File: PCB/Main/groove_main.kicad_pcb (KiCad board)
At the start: 2 copper layers, 214 x 99 mm, 38 parts, among them J1 Left_X, J2 Left_Y, J3 Right_X, J4 Right_Y, J5 Left_X, J6 Left_Y, J7 Right_X, J8 Right_Y, U2 Pico, U3 CD4052B

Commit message: Main PCB progress 50%
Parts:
- removed D20, D21, D22, D23, D24: WS2812B_Unified, groove_pico:WS2812B-2835
- added C1: 0.1uF, Capacitor_SMD:C_0603_1608Metric_Pad1.08x0.95mm_HandSolder, F.Cu at (32.5, 102.5)
- added C2: 0.1uF, Capacitor_SMD:C_0603_1608Metric_Pad1.08x0.95mm_HandSolder, F.Cu at (98.2, 125.0)
- added C3: 0.1uF, Capacitor_SMD:C_0603_1608Metric_Pad1.08x0.95mm_HandSolder, B.Cu at (121.3, 65.2)
- added C4: 0.1uF, Capacitor_SMD:C_0603_1608Metric_Pad1.08x0.95mm_HandSolder, F.Cu at (144.6, 97.4)
- added C5: 0.1uF, Capacitor_SMD:C_0603_1608Metric_Pad1.08x0.95mm_HandSolder, F.Cu at (175.1, 130.9)
- added C6: 0.1uF, Capacitor_SMD:C_0603_1608Metric_Pad1.08x0.95mm_HandSolder, F.Cu at (235.4, 96.5)
- added C7: 0.1uF, Capacitor_SMD:C_0603_1608Metric_Pad1.08x0.95mm_HandSolder, F.Cu at (69.7, 118.3)
- added C8: 0.1uF, Capacitor_SMD:C_0603_1608Metric_Pad1.08x0.95mm_HandSolder, F.Cu at (203.0, 118.7)
- added C9: 0.1uF, Capacitor_SMD:C_0603_1608Metric_Pad1.08x0.95mm_HandSolder, F.Cu at (127.3, 73.4)
- added J10: Left_Y, groove_pico:Solder_3P_S, F.Cu at (73.3, 77.9)
- added J11: Right_X, groove_pico:Solder_3P_S, F.Cu at (197.3, 77.9)
- added J12: Right_Y, groove_pico:Solder_3P_S, F.Cu at (188.3, 77.9)
- added J9: Left_X, groove_pico:Solder_3P_S, F.Cu at (82.3, 77.9)
- added SW1: SWITCH_SPST, groove_pico:EVQP1K05M, F.Cu at (118.3, 88.4)
- added SW2: SWITCH_SPST, groove_pico:EVQP1K05M, F.Cu at (135.3, 88.4)
- added SW3: SWITCH_SPST, groove_pico:EVQP1K05M, F.Cu at (152.3, 88.4)
- added U3: LM4040DBZ-3, Package_TO_SOT_SMD:SOT-23, B.Cu at (128.3, 65.2)
- J1, J2, J3, J4: footprint Connector_PinHeader_1.27mm:PinHeader_1x03_P1.27mm_Vertical -> groove_pico:SH1.25_Thruhole_3P
- J5, J6, J7, J8: footprint Connector_JST:JST_GH_BM03B-GHS-TBT_1x03-1MP_P1.25mm_Vertical -> groove_pico:SH1.25mm_3P_SMD
- R2, R3: moved to B.Cu
- U2: renamed from U3; moved to B.Cu
- moved J8 111.3 mm to (188.3, 83.4), turned to 180 degrees
- moved J7 110.4 mm to (197.3, 83.4), turned to 180 degrees
- moved U2 81.0 mm to (119.3, 61.4)
- moved J5 56.2 mm to (82.3, 83.4), turned to 180 degrees
- moved J6 47.9 mm to (73.3, 83.4), turned to 180 degrees
- moved R2 17.0 mm to (129.3, 60.4), turned to 180 degrees
- moved U1 8.89 mm to (117.3, 81.4)
- moved D8 7.20 mm to (89.4, 89.3), turned to -45 degrees
- moved D19 5.53 mm to (229.4, 89.3), turned to -45 degrees
- moved R3 5.37 mm to (141.3, 60.4)
- moved D14 4.67 mm to (171.3, 113.4)
- moved R1 4.22 mm to (69.0, 71.3)
- moved D2 3.18 mm to (41.3, 89.3)
- moved D6 2.96 mm to (89.4, 137.4), turned to -135 degrees
- moved D17 2.62 mm to (229.4, 137.4), turned to -135 degrees
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- renumbered U2 to U1
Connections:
- D19 pad O: Net-(D19-Out) -> unconnected-(D19-Out-PadO)
- J1 pad 1: +3.3VADC -> GNDREF
- J1 pad 3: GND -> +3.3VADC
- J2 pad 1: +3.3VADC -> GNDREF
- J2 pad 3: GND -> +3.3VADC
- J3 pad 1: +3.3VADC -> GNDREF
- J3 pad 3: GND -> +3.3VADC
- J4 pad 1: +3.3VADC -> GNDREF
- J4 pad 3: GND -> +3.3VADC
- J5 pad 1: +3.3VADC -> GNDREF
- J5 pad 3: GND -> +3.3VADC
- J6 pad 1: +3.3VADC -> GNDREF
- J6 pad 3: GND -> +3.3VADC
- J7 pad 1: +3.3VADC -> GNDREF
- J7 pad 3: GND -> +3.3VADC
- J8 pad 1: +3.3VADC -> GNDREF
- J8 pad 3: GND -> +3.3VADC
- U1 pad 34: unconnected-(U2-GPIO28_ADC2-Pad34) -> GNDREF
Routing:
- net +5V: track 0.00 -> 513.2 mm
- net +3.3VADC: track 0.00 -> 191.1 mm, vias 0 -> 3
- net GNDREF: track 0.00 -> 186.6 mm, vias 0 -> 3
- net /RX: track 0.00 -> 95.6 mm, vias 0 -> 1
- net /RY: track 0.00 -> 91.1 mm, vias 0 -> 1
- net /LY: track 0.00 -> 67.0 mm, vias 0 -> 2
- net /LX: track 0.00 -> 64.4 mm, vias 0 -> 2
- net Net-(D11-Out): track 0.00 -> 62.9 mm, vias 0 -> 2
- net Net-(D8-Out): track 0.00 -> 37.7 mm
- net Net-(USB1-DP1): track 0.00 -> 35.0 mm
- net Net-(USB1-DN1): track 0.00 -> 34.8 mm
- net Net-(D12-Out): track 0.00 -> 32.3 mm, vias 0 -> 2
- net +3V3: track 0.00 -> 27.7 mm
- net Net-(U1-GPIO20): track 0.00 -> 25.5 mm
- net Net-(D4-Out): track 0.00 -> 25.0 mm
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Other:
- outline, holes or cut-outs redrawn

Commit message: Main PCB progress 70%
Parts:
- added D20: WS2812B_Unified, groove_pico:WS2812B-4020, B.Cu at (70.4, 126.1)
- added D21: WS2812B_Unified, groove_pico:WS2812B-4020, B.Cu at (60.2, 126.1)
- added D22: WS2812B_Unified, groove_pico:WS2812B-4020, B.Cu at (52.6, 118.5)
- added D23: WS2812B_Unified, groove_pico:WS2812B-4020, B.Cu at (52.6, 108.3)
- added D24: WS2812B_Unified, groove_pico:WS2812B-4020, B.Cu at (60.2, 100.7)
- added D25: WS2812B_Unified, groove_pico:WS2812B-4020, B.Cu at (70.4, 100.7)
- added D26: WS2812B_Unified, groove_pico:WS2812B-4020, B.Cu at (78.0, 108.3)
- added D27: WS2812B_Unified, groove_pico:WS2812B-4020, B.Cu at (78.0, 118.5)
- added D28: WS2812B_Unified, groove_pico:WS2812B-4020_UP, F.Cu at (76.1, 113.4)
- added D29: WS2812B_Unified, groove_pico:WS2812B-4020_UP, F.Cu at (65.3, 102.6)
- added D30: WS2812B_Unified, groove_pico:WS2812B-4020_UP, F.Cu at (54.5, 113.4)
- added D31: WS2812B_Unified, groove_pico:WS2812B-4020_UP, F.Cu at (65.3, 124.2)
- added D32: WS2812B_Unified, groove_pico:WS2812B-4020, B.Cu at (210.4, 126.1)
- added D33: WS2812B_Unified, groove_pico:WS2812B-4020, B.Cu at (200.2, 126.1)
- added D34: WS2812B_Unified, groove_pico:WS2812B-4020, B.Cu at (192.6, 118.5)
- added D35: WS2812B_Unified, groove_pico:WS2812B-4020, B.Cu at (192.6, 108.3)
- added D36: WS2812B_Unified, groove_pico:WS2812B-4020, B.Cu at (200.2, 100.7)
- added D37: WS2812B_Unified, groove_pico:WS2812B-4020, B.Cu at (210.4, 100.7)
- added D38: WS2812B_Unified, groove_pico:WS2812B-4020, B.Cu at (218.0, 108.3)
- added D39: WS2812B_Unified, groove_pico:WS2812B-4020, B.Cu at (218.0, 118.5)
- added D40: WS2812B_Unified, groove_pico:WS2812B-4020_UP, F.Cu at (216.1, 113.4)
- added D41: WS2812B_Unified, groove_pico:WS2812B-4020_UP, F.Cu at (205.3, 102.6)
- added D42: WS2812B_Unified, groove_pico:WS2812B-4020_UP, F.Cu at (194.5, 113.4)
- added D43: WS2812B_Unified, groove_pico:WS2812B-4020_UP, F.Cu at (205.3, 124.2)
- added J13: SW, groove_pico:Solder_1P, B.Cu at (69.1, 107.3)
- added J14: SW, groove_pico:Solder_1P, B.Cu at (209.1, 107.3)
- added J15: V, groove_pico:Solder_1P, B.Cu at (59.0, 110.4)
- added J16: LED, groove_pico:Solder_1P, B.Cu at (72.7, 119.2)
- added J18: G, groove_pico:Solder_1P, B.Cu at (62.5, 107.5)
- added J19: V, groove_pico:Solder_1P, B.Cu at (199.0, 110.4)
- added J20: LED, groove_pico:Solder_1P, B.Cu at (212.7, 119.2)
- added J22: G, groove_pico:Solder_1P, B.Cu at (202.5, 107.5)
- added R4: 10, Resistor_SMD:R_0603_1608Metric, F.Cu at (41.8, 43.5)
- added R5: 10, Resistor_SMD:R_0603_1608Metric, F.Cu at (41.8, 46.0)
- added SCR1: ScrewHole, groove_pico:Hole2.0, F.Cu at (65.3, 100.2)
- added SCR2: ScrewHole, groove_pico:Hole2.0, F.Cu at (78.5, 113.4)
- added SCR3: ScrewHole, groove_pico:Hole2.0, F.Cu at (65.3, 126.6)
- added SCR4: ScrewHole, groove_pico:Hole2.0, F.Cu at (52.1, 113.4)
- added SCR5: ScrewHole, groove_pico:Hole2.0, F.Cu at (205.3, 100.2)
- added SCR6: ScrewHole, groove_pico:Hole2.0, F.Cu at (218.5, 113.4)
- added SCR7: ScrewHole, groove_pico:Hole2.0, F.Cu at (205.3, 126.6)
- added SCR8: ScrewHole, groove_pico:Hole2.0, F.Cu at (192.1, 113.4)
- added SW4: SWITCH_SPST, groove_pico:SW_Kailh_Choc_V1V2_1.00u_LED, F.Cu at (65.3, 113.4)
- added SW5: SWITCH_SPST, groove_pico:SW_Kailh_Choc_V1V2_1.00u_LED, F.Cu at (205.3, 113.4)
- moved C7 16.1 mm to (65.2, 133.8)
- moved C8 12.9 mm to (205.5, 131.4)
- moved C9 2.06 mm to (126.3, 71.6)
- renumbered R2 to R1, R3 to R2, R1 to R3
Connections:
- SW1 pad 1: unconnected-(SW1-"~{"}-Pad1) -> Net-(U1-GPIO0)
- SW1 pad 2: unconnected-(SW1-"~{"}-Pad2) -> GND
- SW2 pad 1: unconnected-(SW2-"~{"}-Pad1) -> Net-(U1-GPIO1)
- SW2 pad 2: unconnected-(SW2-"~{"}-Pad2) -> GND
- SW3 pad 1: unconnected-(SW3-"~{"}-Pad1) -> Net-(U1-GPIO2)
- SW3 pad 2: unconnected-(SW3-"~{"}-Pad2) -> GND
- U1 pad 1: unconnected-(U1-GPIO0-Pad1) -> Net-(U1-GPIO0)
- U1 pad 13: unconnected-(U1-GND-Pad13) -> GND
- U1 pad 15: unconnected-(U1-GPIO11-Pad15) -> Net-(U1-GPIO11)
- U1 pad 16: /RGB -> Net-(U1-GPIO12)
- U1 pad 17: unconnected-(U1-GPIO13-Pad17) -> /RGB
- U1 pad 2: unconnected-(U1-GPIO1-Pad2) -> Net-(U1-GPIO1)
- U1 pad 23: unconnected-(U1-GND-Pad23) -> GND
- U1 pad 33: unconnected-(U1-AGND-Pad33) -> GNDREF
- U1 pad 34: GNDREF -> unconnected-(U1-GPIO28_ADC2-Pad34)
- U1 pad 4: unconnected-(U1-GPIO2-Pad4) -> Net-(U1-GPIO2)
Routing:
- net +5V: track 513.2 -> 796.8 mm, vias 0 -> 2
- net Net-(D30-Out): track 0.00 -> 16.5 mm
- net Net-(D40-Out): track 0.00 -> 16.5 mm
- net Net-(D28-Out): track 0.00 -> 16.5 mm
- net Net-(D42-Out): track 0.00 -> 16.5 mm
- net Net-(D41-Out): track 0.00 -> 16.3 mm
- net Net-(D29-Out): track 0.00 -> 16.3 mm
- net GND: track 9.07 -> 20.2 mm, vias 6 -> 18
- net Net-(D23-Out): track 0.00 -> 10.6 mm
- net Net-(D35-Out): track 0.00 -> 10.6 mm
- net Net-(D33-Out): track 0.00 -> 10.6 mm
- net Net-(D21-Out): track 0.00 -> 10.6 mm
- net Net-(D37-Out): track 0.00 -> 10.6 mm
- net Net-(D25-Out): track 0.00 -> 10.6 mm
- net Net-(D38-Out): track 0.00 -> 10.1 mm
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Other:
- outline, holes or cut-outs redrawn

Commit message: Main PCB progress 85%
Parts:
- added J17: LED, groove_pico:Solder_1P_S, F.Cu at (59.3, 85.4)
- added J21: LED, groove_pico:Solder_1P_S, F.Cu at (211.3, 85.4)
- added J23: SW, groove_pico:Solder_1P_S, F.Cu at (205.3, 85.4)
- added J24: SW, groove_pico:Solder_1P_S, F.Cu at (65.3, 85.4)
- added J25: V, groove_pico:Solder_1P_S, F.Cu at (214.3, 85.4)
- added J26: V, groove_pico:Solder_1P_S, F.Cu at (56.3, 85.4)
- added J27: G, groove_pico:Solder_1P_S, F.Cu at (62.3, 85.4)
- added J28: G, groove_pico:Solder_1P_S, F.Cu at (208.3, 85.4)
- C7, C8, C9: moved to B.Cu
- J13, J14, J15, J16, J18, J19, J20, J22: footprint groove_pico:Solder_1P -> groove_pico:Solder_1P_S
- moved R5 75.2 mm to (105.9, 85.4), turned to -90 degrees
- moved R4 74.4 mm to (103.3, 85.4), turned to -90 degrees
- moved R3 34.8 mm to (100.8, 85.4), turned to -90 degrees
- moved C7 26.8 mm to (60.1, 107.5)
- moved C8 24.5 mm to (200.0, 107.5)
- moved SW1 6.00 mm to (124.3, 88.4)
- moved SW3 6.00 mm to (146.3, 88.4)
- moved C9 5.92 mm to (128.5, 66.1)
- moved J20 2.93 mm to (211.2, 116.7), turned to -90 degrees
- moved J16 2.85 mm to (71.2, 116.8), turned to -90 degrees
- moved U3 1.75 mm to (128.4, 63.4)
- moved C4 1.64 mm to (143.1, 97.9)
- moved J13 1.01 mm to (68.3, 106.7), turned to 90 degrees
- moved D11 1.00 mm to (151.3, 96.4)
- moved D9 1.00 mm to (119.3, 96.4)
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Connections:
- net /RGB renamed Net-(U1-GPIO13)
- R4 pad 1: Net-(D20-In) -> Net-(J17-Pad1)
- R5 pad 1: Net-(D32-In) -> Net-(J21-Pad1)
- SW1 pad 1: Net-(U1-GPIO0) -> Net-(U1-GPIO2)
- SW3 pad 1: Net-(U1-GPIO2) -> Net-(U1-GPIO0)
- SW4 pad 1: Net-(J13-Pad1) -> GND
- SW4 pad 2: GND -> Net-(J13-Pad1)
- SW5 pad 1: Net-(J14-Pad1) -> GND
- SW5 pad 2: GND -> Net-(J14-Pad1)
- U1 pad 11: unconnected-(U1-GPIO8-Pad11) -> Net-(U1-GPIO8)
- U1 pad 12: unconnected-(U1-GPIO9-Pad12) -> Net-(U1-GPIO9)
- U1 pad 13: GND -> unconnected-(U1-GND-Pad13)
- U1 pad 40: unconnected-(U1-VBUS-Pad40) -> Net-(U1-VBUS)
- U1 pad 8: unconnected-(U1-GND-Pad8) -> GND
- U2 pad 6: unconnected-(U2-INH-Pad6) -> GND
- USB1 pad 11: Net-(USB1-VBUS-Pad11) -> Net-(U1-VBUS)
- USB1 pad 2: Net-(USB1-VBUS-Pad11) -> Net-(U1-VBUS)
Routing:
- net +5V: track 796.8 -> 1057.8 mm, vias 2 -> 8
- net Net-(J21-Pad1): track 0.00 -> 111.1 mm, vias 0 -> 2
- net Net-(U1-GPIO8): track 0.00 -> 98.1 mm, vias 0 -> 1
- net GND: track 20.2 -> 93.0 mm, vias 18 -> 80
- net Net-(U1-GPIO9): track 0.00 -> 53.3 mm, vias 0 -> 1
- net Net-(J17-Pad1): track 0.00 -> 51.0 mm, vias 0 -> 2
- net Net-(D1-In): track 0.00 -> 39.7 mm, vias 0 -> 2
- net Net-(U1-VBUS): track 0.00 -> 26.0 mm, vias 0 -> 2
- net Net-(U1-GPIO2): track 0.00 -> 18.4 mm, vias 0 -> 1
- net unconnected-(USB1-SHIELD-Pad13): track 0.00 -> 17.0 mm
- net Net-(U1-GPIO1): track 0.00 -> 15.5 mm, vias 0 -> 1
- net Net-(U1-GPIO0): track 0.00 -> 15.2 mm, vias 0 -> 1
- net GNDREF: track 187.3 -> 194.3 mm
- net +3.3VADC: track 190.6 -> 197.2 mm
- net Net-(USB1-CC2): track 5.54 -> 11.6 mm
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- added copper zone on B.Cu, net GND
- added copper zone on F.Cu, net GND

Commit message: Main PCB v1.0
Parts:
- added SCR10: ScrewHole, groove_pico:Hole2.0, F.Cu at (221.3, 81.4)
- added SCR11: ScrewHole, groove_pico:Hole2.0, F.Cu at (165.3, 59.4)
- added SCR12: ScrewHole, groove_pico:Hole2.0, F.Cu at (109.3, 97.4)
- added SCR13: ScrewHole, groove_pico:Hole2.0, F.Cu at (49.3, 81.4)
- added SCR14: ScrewHole, groove_pico:Hole2.0, F.Cu at (161.3, 97.4)
- added SCR15: ScrewHole, groove_pico:Hole2.0, F.Cu at (65.3, 141.4)
- added SCR16: ScrewHole, groove_pico:Hole2.0, F.Cu at (205.3, 141.4)
- added SCR9: ScrewHole, groove_pico:Hole2.0, F.Cu at (105.3, 59.4)
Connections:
- J13 pad 1: Net-(J13-Pad1) -> /SW_L
- J14 pad 1: Net-(J14-Pad1) -> /SW_R
- J17 pad 1: Net-(J17-Pad1) -> Net-(D20-In)
- J21 pad 1: Net-(J21-Pad1) -> Net-(D32-In)
- J23 pad 1: Net-(U1-GPIO8) -> /SW_R
- J24 pad 1: Net-(U1-GPIO9) -> /SW_L
- R4 pad 1: Net-(J17-Pad1) -> Net-(D20-In)
- R5 pad 1: Net-(J21-Pad1) -> Net-(D32-In)
- SW4 pad 2: Net-(J13-Pad1) -> /SW_L
- SW5 pad 2: Net-(J14-Pad1) -> /SW_R
- U1 pad 11: Net-(U1-GPIO8) -> /SW_R
- U1 pad 12: Net-(U1-GPIO9) -> /SW_L
- U1 pad 28: unconnected-(U1-GND-Pad28) -> GND
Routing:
- net Net-(D32-In): track 9.84 -> 178.5 mm, vias 0 -> 4
- net /SW_R: track 0.00 -> 131.8 mm, vias 0 -> 2
- net Net-(J21-Pad1): track 111.1 -> 0.00 mm, vias 2 -> 0
- net Net-(D20-In): track 9.74 -> 115.5 mm, vias 0 -> 4
- net Net-(U1-GPIO8): track 98.1 -> 0.00 mm, vias 1 -> 0
- net /SW_L: track 0.00 -> 87.8 mm, vias 0 -> 3
- net Net-(U1-GPIO9): track 53.3 -> 0.00 mm, vias 1 -> 0
- net Net-(J17-Pad1): track 51.0 -> 0.00 mm, vias 2 -> 0
- net +5V: track 1057.8 -> 1052.1 mm
- net Net-(J13-Pad1): track 4.49 -> 0.00 mm
- net Net-(J14-Pad1): track 4.39 -> 0.00 mm
- net Net-(D41-Out): track 16.3 -> 13.9 mm
- net Net-(D29-Out): track 16.3 -> 13.9 mm
- net Net-(D8-Out): track 38.6 -> 39.2 mm
- net GND: track 93.0 -> 93.2 mm, vias 80 -> 83
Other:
- board text added: "Groove Pico v1.0"

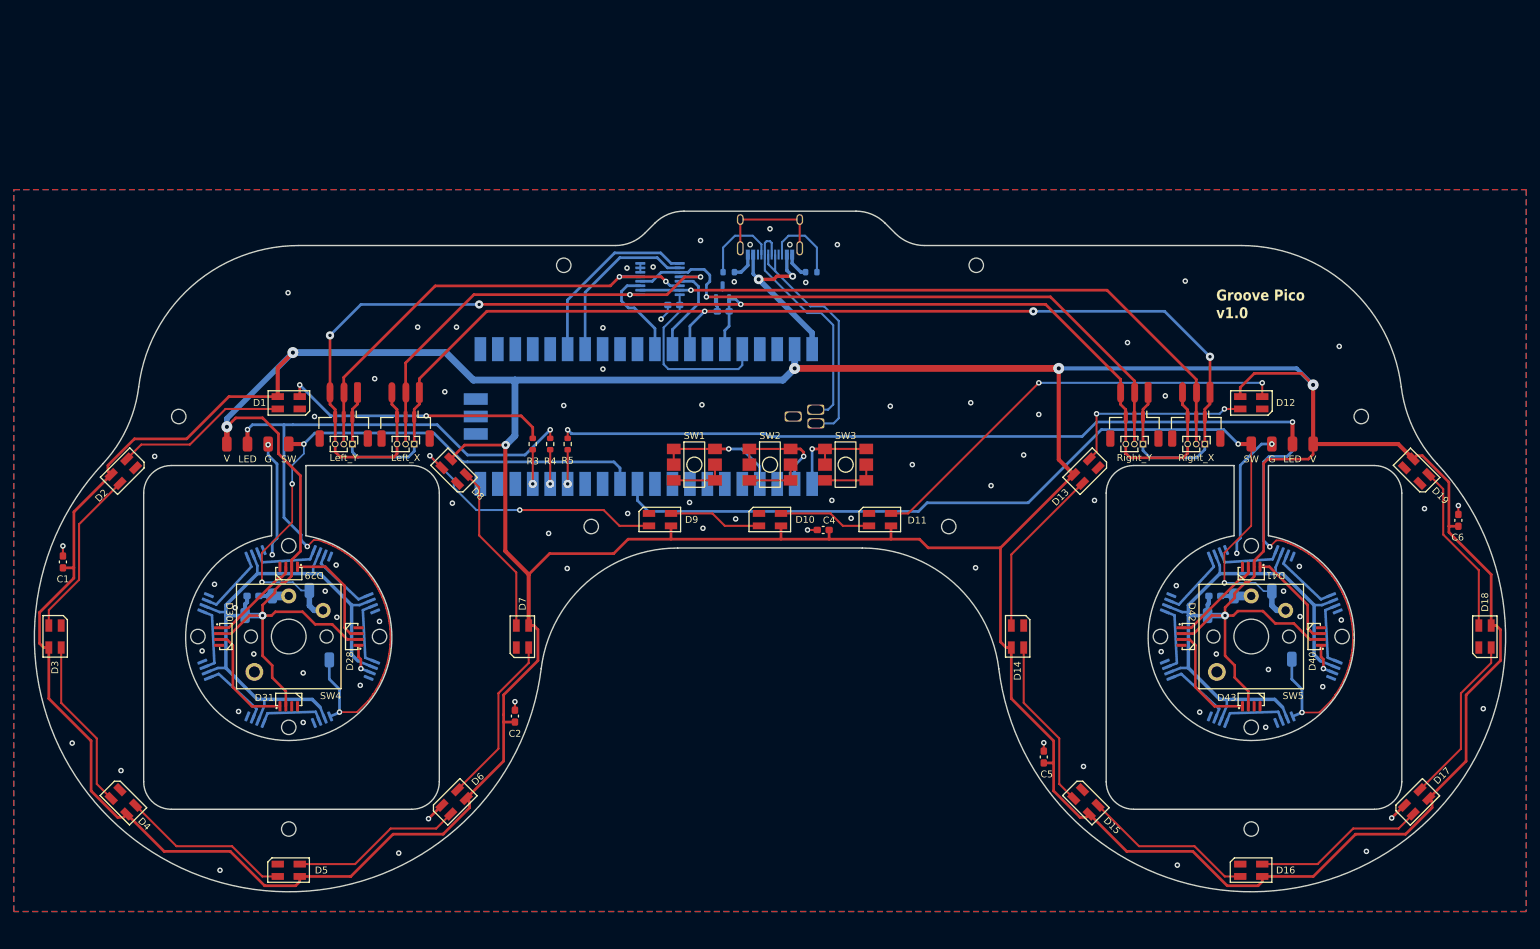
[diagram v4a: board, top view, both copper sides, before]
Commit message: Add slots in PCB for Hall gimbals
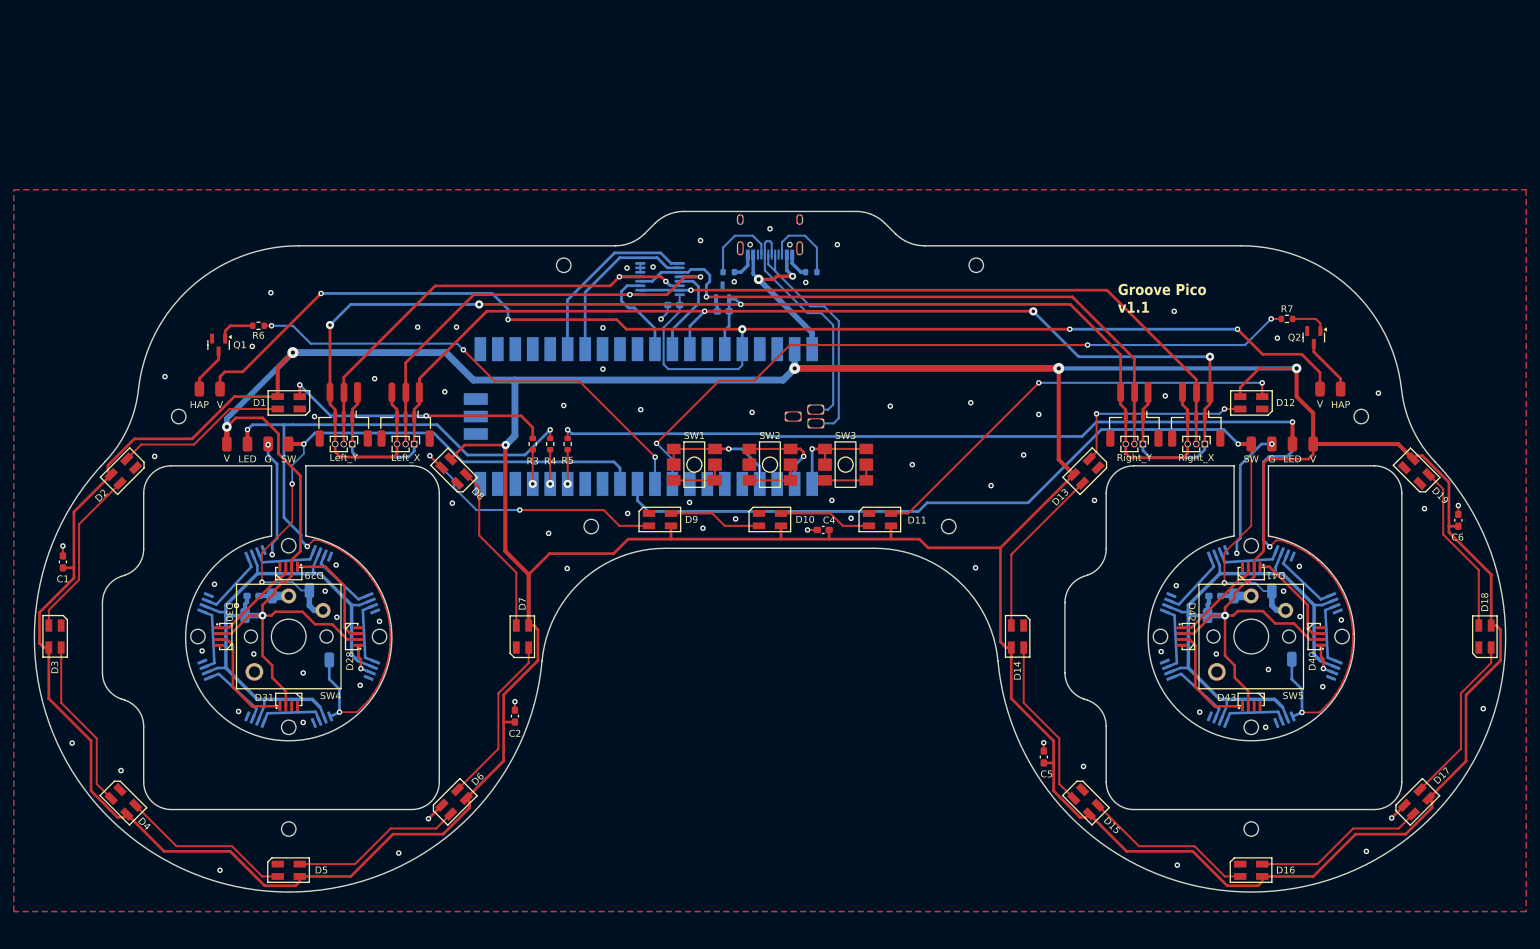
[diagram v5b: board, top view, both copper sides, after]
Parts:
- added J29: HAP, groove_pico:Solder_1P_S, F.Cu at (52.3, 77.4)
- added J30: V, groove_pico:Solder_1P_S, F.Cu at (55.3, 77.4)
- added J31: HAP, groove_pico:Solder_1P_S, F.Cu at (218.3, 77.4)
- added J32: V, groove_pico:Solder_1P_S, F.Cu at (215.3, 77.4)
- added Q1: AO3400A, Package_TO_SOT_SMD:SOT-23, F.Cu at (55.1, 71.0)
- added Q2: AO3400A, Package_TO_SOT_SMD:SOT-23, F.Cu at (214.4, 69.9)
- added R6: 10R, Resistor_SMD:R_0603_1608Metric, F.Cu at (60.9, 68.2)
- added R7: 10R, Resistor_SMD:R_0603_1608Metric, F.Cu at (210.5, 67.2)
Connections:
- U1 pad 10: unconnected-(U1-GPIO7-Pad10) -> /TAP_L
- U1 pad 9: unconnected-(U1-GPIO6-Pad9) -> /TAP_R
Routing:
- net +3V3: track 25.4 -> 203.1 mm, vias 0 -> 5
- net /TAP_R: track 0.00 -> 105.2 mm, vias 0 -> 3
- net /TAP_L: track 0.00 -> 68.7 mm, vias 0 -> 3
- net unconnected-(USB1-SHIELD-Pad13): track 17.0 -> 0.00 mm
- net Net-(Q2-D): track 0.00 -> 7.88 mm
- net Net-(Q1-D): track 0.00 -> 6.32 mm
- net Net-(Q1-G): track 0.00 -> 5.45 mm
- net Net-(Q2-G): track 0.00 -> 5.41 mm
- net +3.3VADC: track 197.2 -> 200.2 mm
- net +5V: track 1052.1 -> 1049.3 mm
- net /RY: track 91.1 -> 92.9 mm
- net GND: vias 83 -> 86
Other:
- outline, holes or cut-outs redrawn
- board text added: "Groove Pico v1.1"
- board text removed: "Groove Pico v1.0"

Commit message: Main PCB v1.1
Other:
- outline, holes or cut-outs redrawn
